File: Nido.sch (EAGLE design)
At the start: 9 parts, among them J1 2X6 FEMALE, K1 HE3621, T1 BC337, U1 BME280

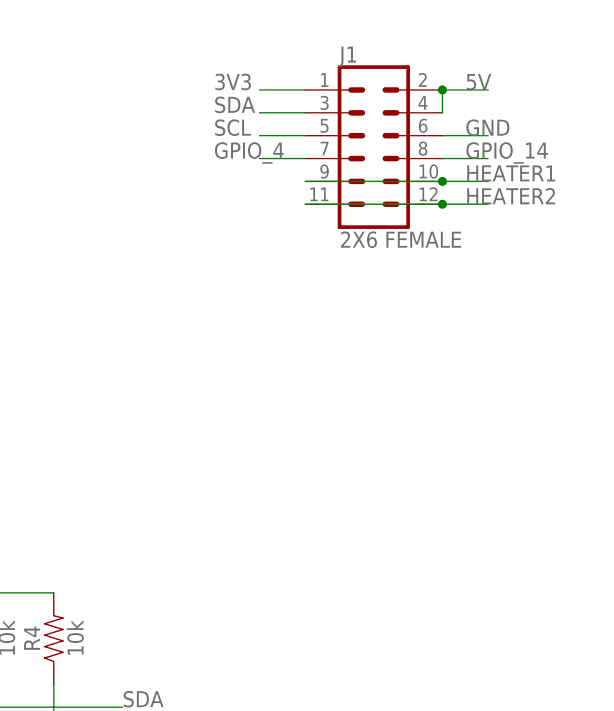
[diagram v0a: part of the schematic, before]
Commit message: Updated board components, added PCB photos
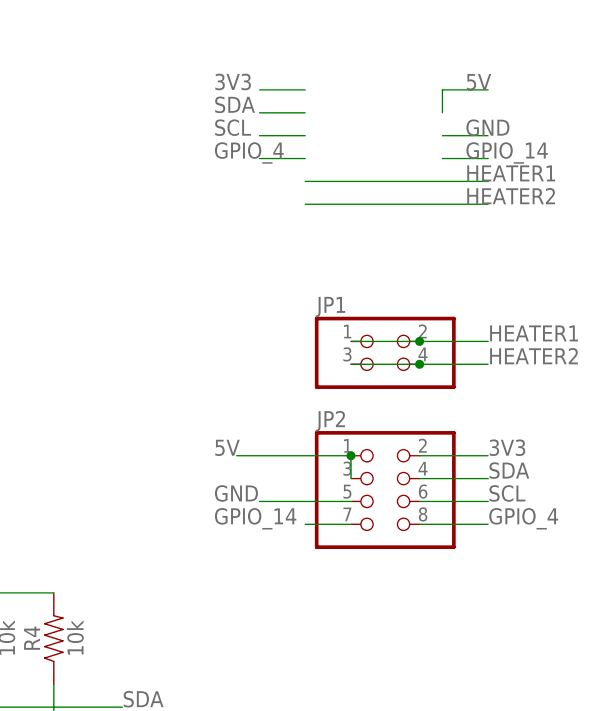
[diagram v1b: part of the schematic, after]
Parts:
- removed J1: 2X6 FEMALE, SparkFun-Connectors:CONN_06X2PTH_FEMALE
- added JP1: (no value), pinhead:PINHD-2X2
- added JP2: (no value), pinhead:PINHD-2X4
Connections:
- net 3V3: now also JP2.2; no longer J1.1
- net 5V: now also JP2.1, JP2.3; no longer J1.2, J1.4
- net GND: now also JP2.5; no longer J1.6
- net GPIO_14: now also JP2.7; no longer J1.8
- net GPIO_4: now also JP2.8; no longer J1.7
- net HEATER1: now also JP1.1, JP1.2; no longer J1.10, J1.9
- net HEATER2: now also JP1.3, JP1.4; no longer J1.11, J1.12
- net SCL: now also JP2.6; no longer J1.5
- net SDA: now also JP2.4; no longer J1.3
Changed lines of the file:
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@@
 <part name="R1" library="SparkFun-Resistors" deviceset="1KOHM" device="-HORIZ-1/4W-1%" value="10k"/>
 <part name="T1" library="transistor" library_urn="urn:adsk.eagle:library:402" deviceset="BC337" device="" package3d_urn="urn:adsk.eagle:package:28523/2"/>
-<part name="J1" library="SparkFun-Connectors" deviceset="CONN_06X2" device="PTH_FEMALE" value="2X6 FEMALE"/>
 <part name="U1" library="SparkFun-Sensors" deviceset="BME280" device="" value="BME280"/>
 <part name="R2" library="SparkFun-Resistors" deviceset="1KOHM" device="-HORIZ-1/4W-1%" value="10k"/>
@@
 <part name="GND2" library="SparkFun-PowerSymbols" deviceset="GND" device=""/>
 <part name="5V" library="SparkFun-PowerSymbols" deviceset="5V" device=""/>
+<part name="JP1" library="pinhead" library_urn="urn:adsk.eagle:library:325" deviceset="PINHD-2X2" device="" package3d_urn="urn:adsk.eagle:package:22455/2"/>
+<part name="JP2" library="pinhead" library_urn="urn:adsk.eagle:library:325" deviceset="PINHD-2X4" device="" package3d_urn="urn:adsk.eagle:package:22461/2"/>
 </parts>
 <sheets>
@@
 <attribute name="VALUE" x="43.18" y="142.24" size="1.778" layer="96"/>
 </instance>
-<instance part="J1" gate="G$1" x="111.76" y="154.94" smashed="yes">
-<attribute name="VALUE" x="110.49" y="150.114" size="1.778" layer="96" font="vector"/>
-<attribute name="NAME" x="110.49" y="170.688" size="1.778" layer="95" font="vector"/>
-</instance>
 <instance part="U1" gate="U1" x="38.1" y="99.06" smashed="yes">
 <attribute name="NAME" x="27.94" y="106.934" size="1.778" layer="95"/>
@@
 <instance part="5V" gate="G$1" x="40.64" y="170.18" smashed="yes">
 <attribute name="VALUE" x="40.64" y="172.974" size="1.778" layer="96" align="bottom-center"/>
+</instance>
+<instance part="JP1" gate="A" x="116.84" y="137.16" smashed="yes">
+<attribute name="NAME" x="107.95" y="142.875" size="1.778" layer="95"/>
+<attribute name="VALUE" x="107.95" y="132.08" size="1.778" layer="96"/>
+</instance>
+<instance part="JP2" gate="A" x="114.3" y="121.92" smashed="yes">
+<attribute name="NAME" x="107.95" y="130.175" size="1.778" layer="95"/>
+<attribute name="VALUE" x="107.95" y="114.3" size="1.778" layer="96"/>
 </instance>
 </instances>
@@
 <net name="3V3" class="0">
 <segment>
-<pinref part="J1" gate="G$1" pin="1"/>
 <wire x1="106.68" y1="167.64" x2="101.6" y2="167.64" width="0.1524" layer="91"/>
 <label x="96.52" y="167.64" size="1.778" layer="95"/>
@@
 <junction x="22.86" y="111.76"/>
 </segment>
+<segment>
+<pinref part="JP2" gate="A" pin="2"/>
+<wire x1="119.38" y1="127" x2="127" y2="127" width="0.1524" layer="91"/>
+<label x="127" y="127" size="1.778" layer="95"/>
+</segment>
 </net>
 <net name="SDA" class="0">
 <segment>
-<pinref part="J1" gate="G$1" pin="3"/>
 <wire x1="106.68" y1="165.1" x2="101.6" y2="165.1" width="0.1524" layer="91"/>
 <label x="96.52" y="165.1" size="1.778" layer="95"/>
@@
 <label x="86.36" y="99.06" size="1.778" layer="95"/>
 </segment>
+<segment>
+<pinref part="JP2" gate="A" pin="4"/>
+<wire x1="119.38" y1="124.46" x2="127" y2="124.46" width="0.1524" layer="91"/>
+<label x="127" y="124.46" size="1.778" layer="95"/>
+</segment>
 </net>
 <net name="SCL" class="0">
 <segment>
-<pinref part="J1" gate="G$1" pin="5"/>
 <wire x1="106.68" y1="162.56" x2="101.6" y2="162.56" width="0.1524" layer="91"/>
 <label x="96.52" y="162.56" size="1.778" layer="95"/>
@@
 <label x="86.36" y="96.52" size="1.778" layer="95"/>
 </segment>
+<segment>
+<pinref part="JP2" gate="A" pin="6"/>
+<wire x1="119.38" y1="121.92" x2="127" y2="121.92" width="0.1524" layer="91"/>
+<label x="127" y="121.92" size="1.778" layer="95"/>
+</segment>
 </net>
 <net name="GPIO_4" class="0">
 <segment>
-<pinref part="J1" gate="G$1" pin="7"/>
 <wire x1="106.68" y1="160.02" x2="101.6" y2="160.02" width="0.1524" layer="91"/>
 <label x="96.52" y="160.02" size="1.778" layer="95"/>
@@
 <label x="15.24" y="152.4" size="1.778" layer="95"/>
 </segment>
+<segment>
+<pinref part="JP2" gate="A" pin="8"/>
+<wire x1="119.38" y1="119.38" x2="127" y2="119.38" width="0.1524" layer="91"/>
+<label x="127" y="119.38" size="1.778" layer="95"/>
+</segment>
 </net>
 <net name="5V" class="0">
 <segment>
-<pinref part="J1" gate="G$1" pin="2"/>
 <wire x1="121.92" y1="167.64" x2="127" y2="167.64" width="0.1524" layer="91"/>
 <label x="124.46" y="167.64" size="1.778" layer="95"/>
-<pinref part="J1" gate="G$1" pin="4"/>
 <wire x1="121.92" y1="167.64" x2="121.92" y2="165.1" width="0.1524" layer="91"/>
-<junction x="121.92" y="167.64"/>
 </segment>
 <segment>
@@
 <wire x1="40.64" y1="170.18" x2="40.64" y2="165.1" width="0.1524" layer="91"/>
 </segment>
+<segment>
+<pinref part="JP2" gate="A" pin="1"/>
+<wire x1="111.76" y1="127" x2="99.06" y2="127" width="0.1524" layer="91"/>
+<pinref part="JP2" gate="A" pin="3"/>
+<wire x1="111.76" y1="124.46" x2="111.76" y2="127" width="0.1524" layer="91"/>
+<junction x="111.76" y="127"/>
+<label x="96.52" y="127" size="1.778" layer="95"/>
+</segment>
 </net>
 <net name="GND" class="0">
 <segment>
-<pinref part="J1" gate="G$1" pin="6"/>
 <wire x1="121.92" y1="162.56" x2="127" y2="162.56" width="0.1524" layer="91"/>
 <label x="124.46" y="162.56" size="1.778" layer="95"/>
@@
 <junction x="20.32" y="91.44"/>
 </segment>
+<segment>
+<pinref part="JP2" gate="A" pin="5"/>
+<wire x1="111.76" y1="121.92" x2="101.6" y2="121.92" width="0.1524" layer="91"/>
+<label x="96.52" y="121.92" size="1.778" layer="95"/>
+</segment>
 </net>
 <net name="GPIO_14" class="0">
 <segment>
-<pinref part="J1" gate="G$1" pin="8"/>
 <wire x1="121.92" y1="160.02" x2="127" y2="160.02" width="0.1524" layer="91"/>
 <label x="124.46" y="160.02" size="1.778" layer="95"/>
 </segment>
+<segment>
+<pinref part="JP2" gate="A" pin="7"/>
+<wire x1="111.76" y1="119.38" x2="106.68" y2="119.38" width="0.1524" layer="91"/>
+<label x="96.52" y="119.38" size="1.778" layer="95"/>
+</segment>
 </net>
 <net name="HEATER1" class="0">
 <segment>
-<pinref part="J1" gate="G$1" pin="10"/>
-<wire x1="121.92" y1="157.48" x2="127" y2="157.48" width="0.1524" layer="91"/>
 <label x="124.46" y="157.48" size="1.778" layer="95"/>
-<pinref part="J1" gate="G$1" pin="9"/>
-<wire x1="106.68" y1="157.48" x2="121.92" y2="157.48" width="0.1524" layer="91"/>
-<junction x="121.92" y="157.48"/>
+<wire x1="106.68" y1="157.48" x2="127" y2="157.48" width="0.1524" layer="91"/>
 </segment>
 <segment>
@@
 <label x="60.96" y="165.1" size="1.778" layer="95"/>
 </segment>
+<segment>
+<pinref part="JP1" gate="A" pin="2"/>
+<wire x1="119.38" y1="139.7" x2="127" y2="139.7" width="0.1524" layer="91"/>
+<label x="127" y="139.7" size="1.778" layer="95"/>
+<pinref part="JP1" gate="A" pin="1"/>
+<wire x1="111.76" y1="139.7" x2="119.38" y2="139.7" width="0.1524" layer="91"/>
+<junction x="119.38" y="139.7"/>
+</segment>
 </net>
 <net name="HEATER2" class="0">
 <segment>
-<pinref part="J1" gate="G$1" pin="12"/>
-<wire x1="121.92" y1="154.94" x2="127" y2="154.94" width="0.1524" layer="91"/>
 <label x="124.46" y="154.94" size="1.778" layer="95"/>
-<pinref part="J1" gate="G$1" pin="11"/>
-<wire x1="106.68" y1="154.94" x2="121.92" y2="154.94" width="0.1524" layer="91"/>
-<junction x="121.92" y="154.94"/>
+<wire x1="106.68" y1="154.94" x2="127" y2="154.94" width="0.1524" layer="91"/>
 </segment>
 <segment>
@@
 <label x="60.96" y="154.94" size="1.778" layer="95"/>
 </segment>
-</net>
+<segment>
+<pinref part="JP1" gate="A" pin="4"/>
+<wire x1="119.38" y1="137.16" x2="127" y2="137.16" width="0.1524" layer="91"/>
+<label x="127" y="137.16" size="1.778" layer="95"/>
+<pinref part="JP1" gate="A" pin="3"/>
+<wire x1="111.76" y1="137.16" x2="119.38" y2="137.16" width="0.1524" layer="91"/>
+<junction x="119.38" y="137.16"/>
+</segment>
+</net>
